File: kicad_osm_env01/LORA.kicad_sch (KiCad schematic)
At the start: 14 parts, among them U16 RAK3172

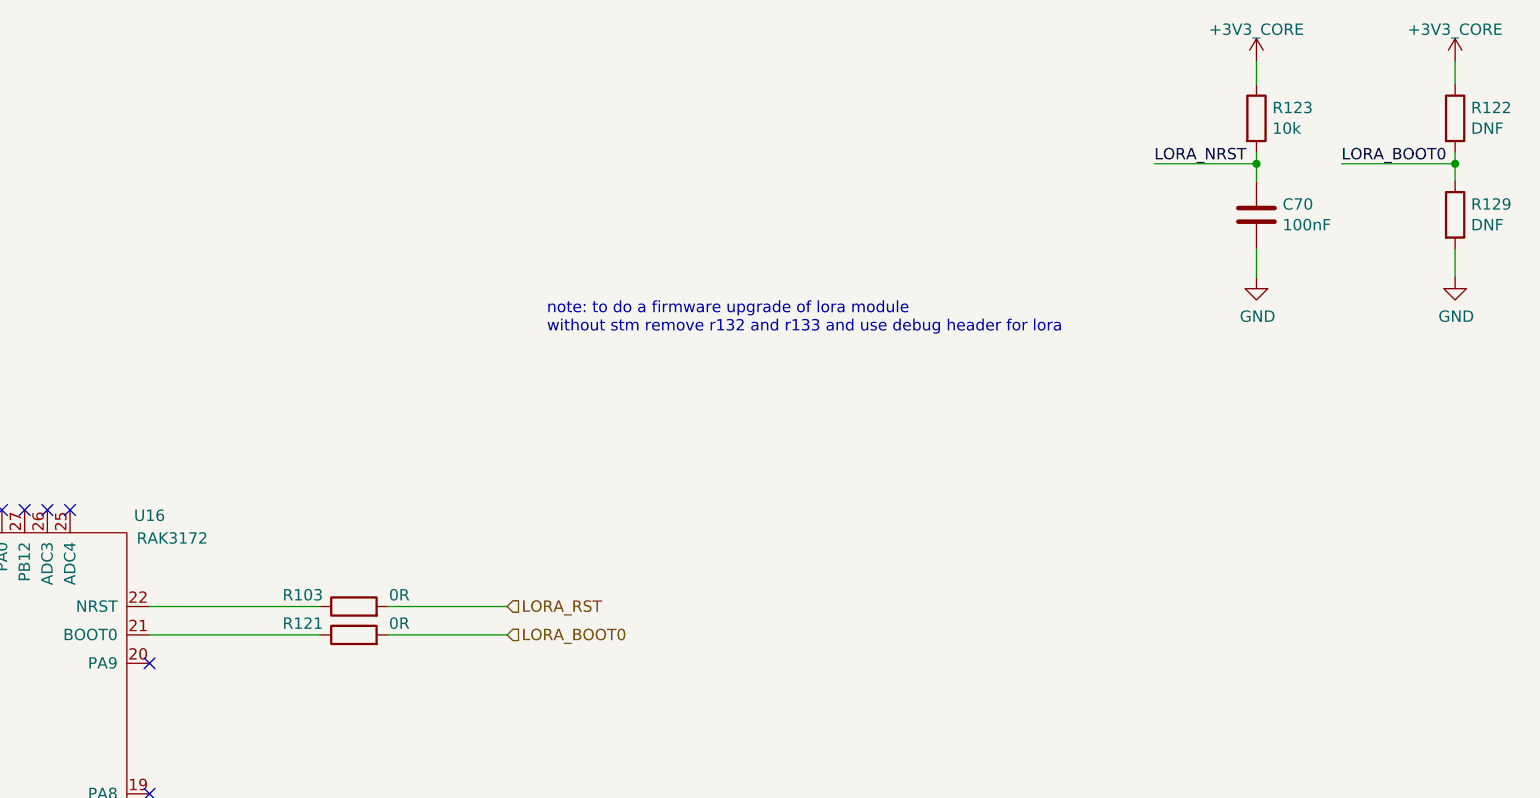
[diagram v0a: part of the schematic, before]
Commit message: updated changes document with xnor power mod and updated schematics with mods so far for osm rev c
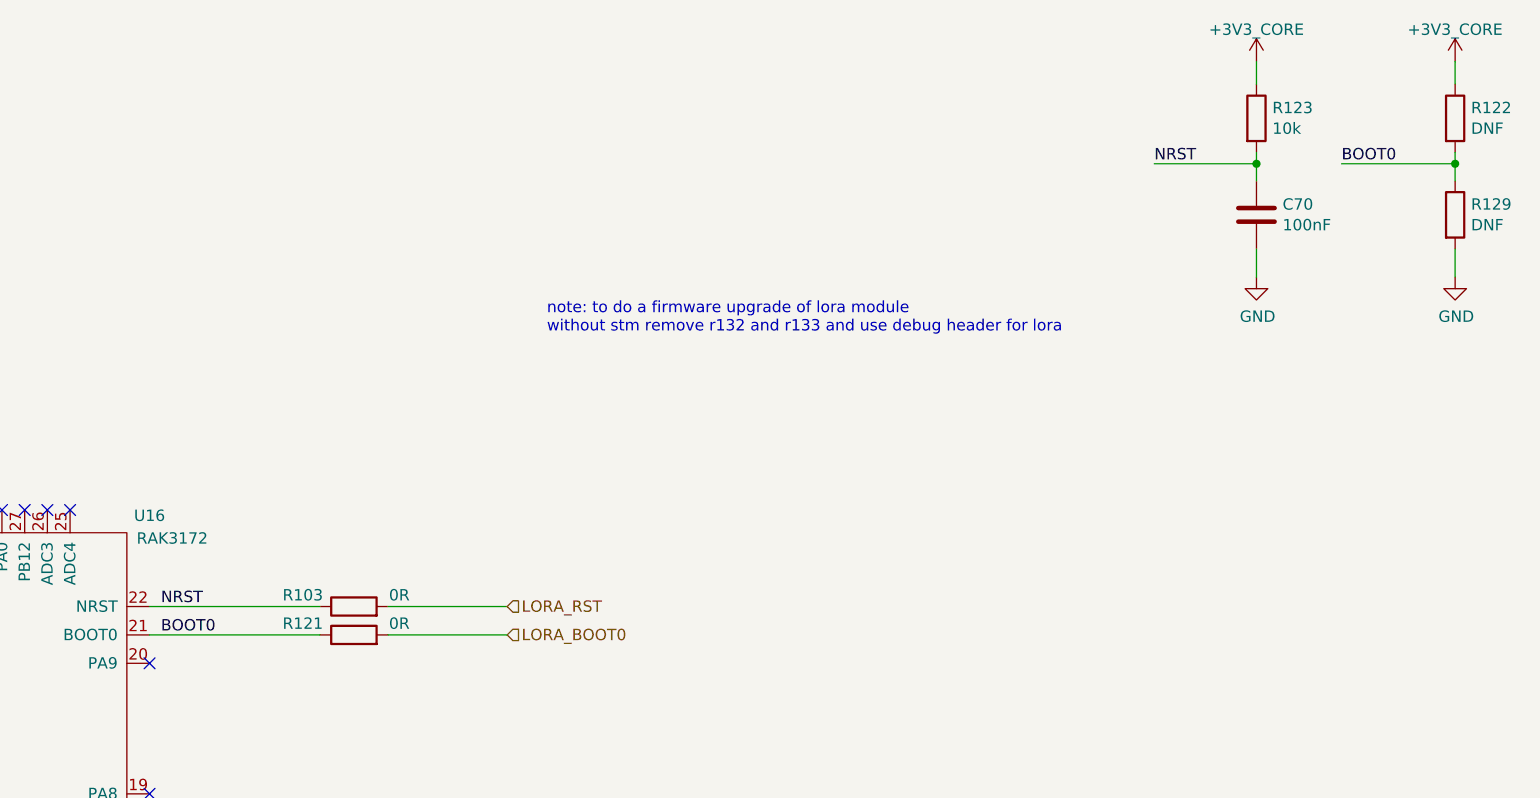
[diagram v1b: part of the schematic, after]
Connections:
- net LORA_NRST is gone; now on net NRST: C70.1, R123.2
- net LORA_BOOT0: no longer R122.2, R129.1
- net NRST: now reaches R103.1, U16.22 (NRST)
- net BOOT0: now reaches R121.1, U16.21 (BOOT0)
- net BOOT0: now also R122.2, R129.1
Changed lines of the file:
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@@
     (effects (font (size 1.27 1.27)) (justify left bottom))
   )
-  (label "LORA_BOOT0" (at 257.81 33.02 0)
+  (label "NRST" (at 125.73 82.55 0)
     (effects (font (size 1.27 1.27)) (justify left bottom))
   )
-  (label "LORA_NRST" (at 236.855 33.02 0)
+  (label "BOOT0" (at 257.81 33.02 0)
     (effects (font (size 1.27 1.27)) (justify left bottom))
   )
+  (label "BOOT0" (at 125.73 85.725 0)
+    (effects (font (size 1.27 1.27)) (justify left bottom))
+  )
+  (label "NRST" (at 236.855 33.02 0)
+    (effects (font (size 1.27 1.27)) (justify left bottom))
+  )
